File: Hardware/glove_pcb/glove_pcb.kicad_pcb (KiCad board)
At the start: 4 copper layers, 144.6 x 80.7 mm, 124 parts, among them J1 OSTVN02A150, J2 OSTVN02A150, J3 54-00130, J4 0430451000, J5 302-R141, J6 302-R141, J7 61300611121, J8 67997-206HLF, J9 22053061, M1 MountingHole_3.5mm_Pad, M2 MountingHole_3.5mm_Pad, M3 MountingHole_3.5mm_Pad, M4 MountingHole_3.5mm_Pad, U1 AP63205WU, U10 BZA408B, U11 BZA408B, U12 MCP3008, U13 ATmega328PB-A, U14 MCP3008, U15 MCP3008, U16 BM70BLES1FC2-0B04AA, U17 MCP111T-195I/TT, U18 74LVC1T45GW_125, U19 74LVC1T45GW_125, U2 TCR2EF33_LMCT, U3 DRV8876PWPR, U4 DRV8876PWPR, U5 DRV8876PWPR, U6 DRV8876PWPR, U7 DRV8876PWPR, U8 BZA408B, U9 BZA408B

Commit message: More routing re-work and cleanup
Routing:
- net MISO: track 10.1 -> 55.7 mm, vias 0 -> 2
- net +5V: track 124.8 -> 92.8 mm, vias 32 -> 33
- net MOSI: track 17.6 -> 49.3 mm
- net GND: track 269.0 -> 258.5 mm, vias 96 -> 95
- net SCK1: track 152.5 -> 143.8 mm
- net UC_PERIPHERAL_SLEEP_RESET: track 222.6 -> 227.3 mm
- net UC_MOTOR_PH3: track 138.6 -> 135.9 mm, vias 4 -> 6
- net SCK: track 47.0 -> 49.2 mm, vias 4 -> 3
- net POT_AREF: track 53.5 -> 51.6 mm
- net SS_ADC2: track 43.8 -> 45.5 mm, vias 7 -> 6
- net MISO1: track 145.9 -> 147.5 mm
- net SS_ADC1: track 24.8 -> 26.4 mm
- net SS_ADC3: track 69.0 -> 70.1 mm
- net OC1B: track 84.9 -> 83.8 mm
- net OC1A: track 90.0 -> 89.0 mm
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
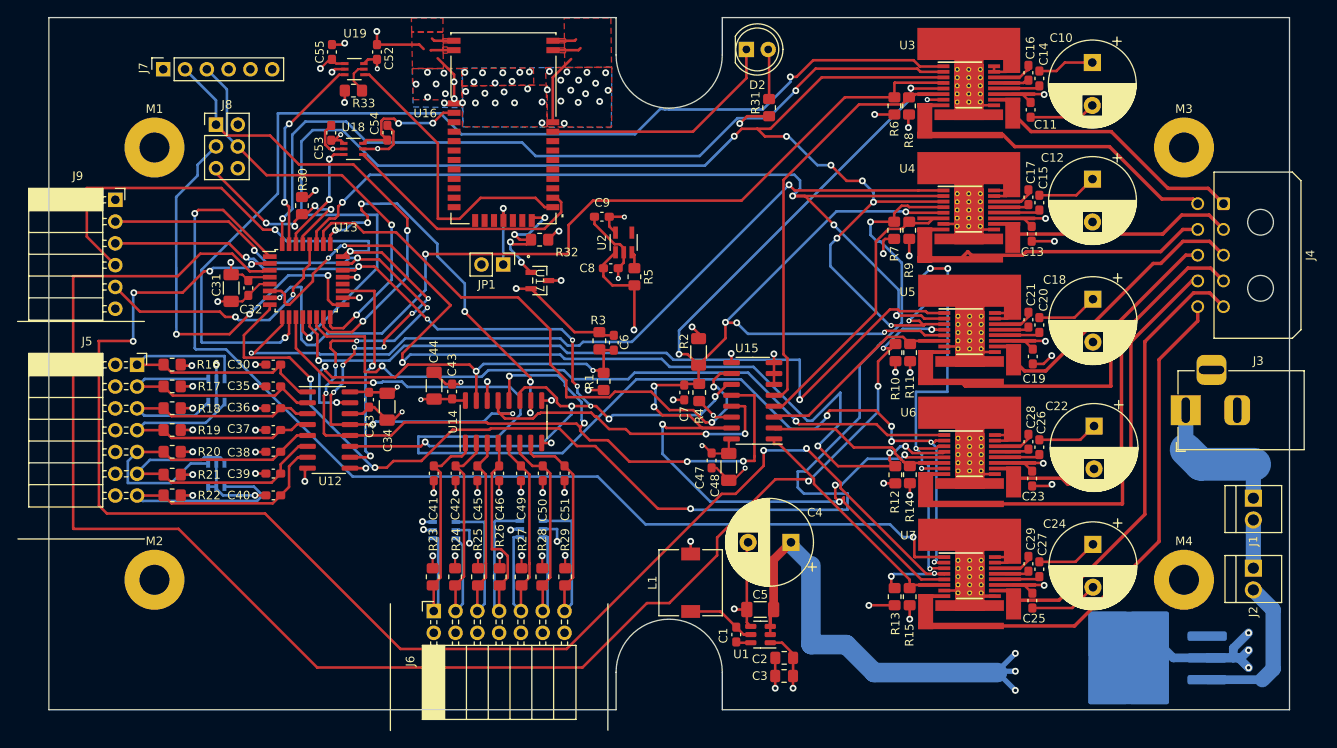
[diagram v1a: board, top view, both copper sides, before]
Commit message: Improving routing to voltage regulators
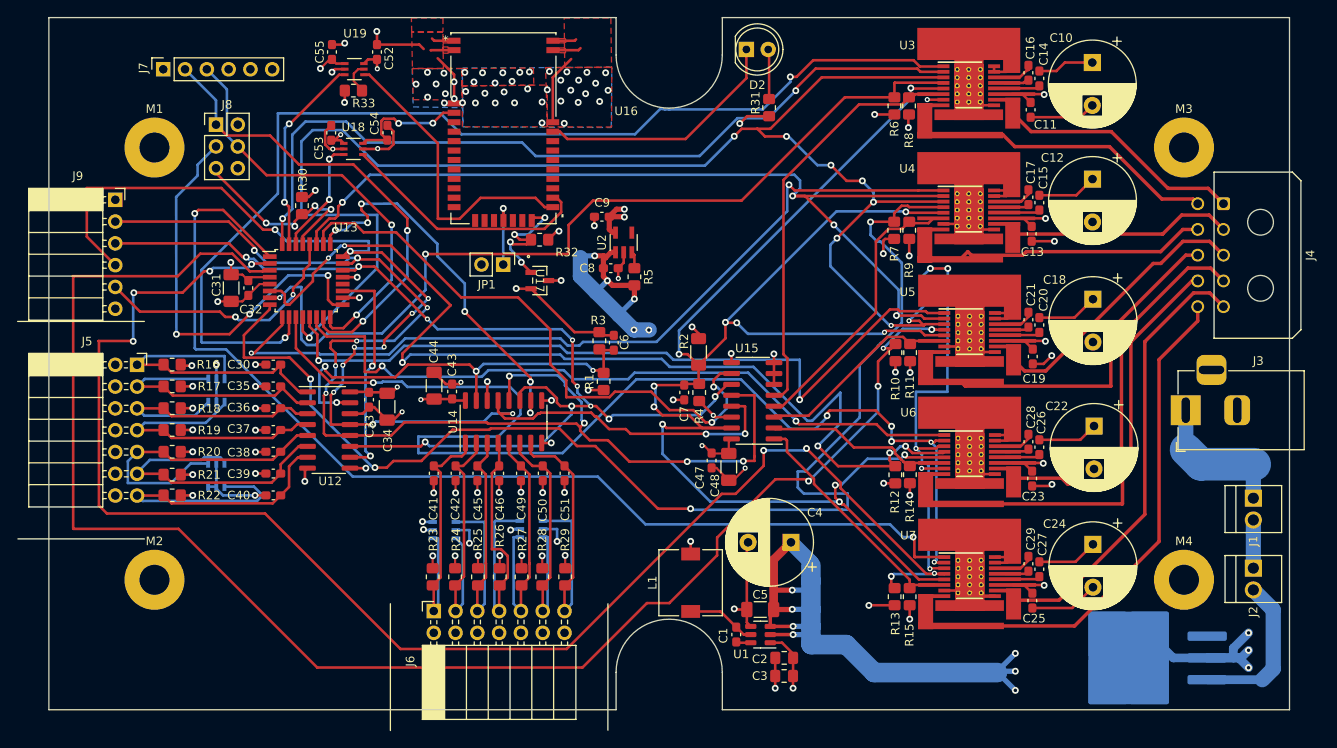
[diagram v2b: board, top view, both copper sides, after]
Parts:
- U16: footprint Glove_Footprints:BM70BLES1FC2_MCH(2) -> Glove_Footprints:BM70BLES1FC2_MCH
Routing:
- net +12V: track 146.7 -> 164.3 mm, vias 11 -> 15
- net +5V: track 92.8 -> 109.9 mm, vias 33 -> 37
- net GND: track 258.5 -> 254.4 mm, vias 95 -> 96
- net +3.3V: track 28.7 -> 31.1 mm, vias 7 -> 8
- net OC0B: track 95.8 -> 97.5 mm
- net MOTOR_AREF: track 201.1 -> 200.4 mm
- net Net-(D2-K): track 28.5 -> 29.2 mm

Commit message: Clearance should be fixed as well as tracks for motors were increased
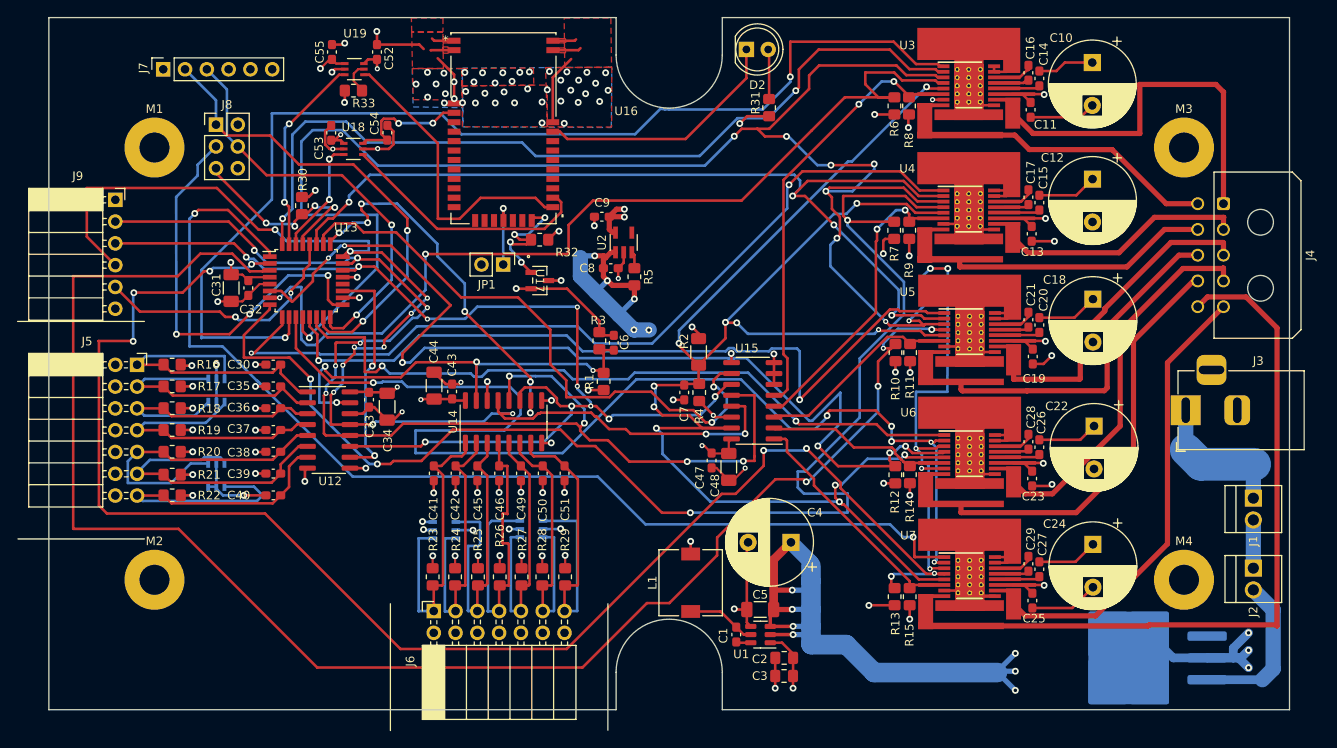
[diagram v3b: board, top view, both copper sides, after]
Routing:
- net MOTOR5_OUT1: track 56.4 -> 82.9 mm
- net MOTOR1_OUT2: track 28.9 -> 44.7 mm
- net UC_PERIPHERAL_SLEEP_RESET: track 227.3 -> 240.9 mm
- net MOTOR2_FAULT: track 147.2 -> 159.4 mm
- net MOTOR1_FAULT: track 103.5 -> 111.1 mm
- net MOTOR3_OUT2: track 31.9 -> 38.4 mm
- net OC0A: track 125.9 -> 129.8 mm
- net MOSI1: track 128.7 -> 132.2 mm
- net POT_MIDDLE_3: track 32.5 -> 35.9 mm
- net POT_PINKY_3: track 37.7 -> 40.7 mm
- net UC_MOTOR_PH1: track 96.0 -> 98.9 mm
- net POT_RING_3: track 35.4 -> 38.3 mm
- net POT_RING_1: track 31.1 -> 33.9 mm
- net POT_PINKY_2: track 31.5 -> 34.2 mm
- net MOTOR2_ISEN: track 32.6 -> 35.0 mm, vias 0 -> 2
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
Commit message: Silkscreen cleanup and final fixes
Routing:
- net MOTOR5_OUT1: track 82.9 -> 57.7 mm
- net POT_MIDDLE_2: track 43.7 -> 36.5 mm
- net MOTOR5_OUT2: track 52.3 -> 56.9 mm
- net GND: track 252.5 -> 250.9 mm, vias 96 -> 93
- net POT_AREF: track 53.3 -> 52.0 mm
- net POT_RING_3: track 38.3 -> 37.3 mm
- net POT_MIDDLE_1: track 34.2 -> 35.1 mm
- net MOTOR3_OUT2: track 38.4 -> 37.6 mm
- net MOTOR4_OUT1: track 47.6 -> 48.2 mm

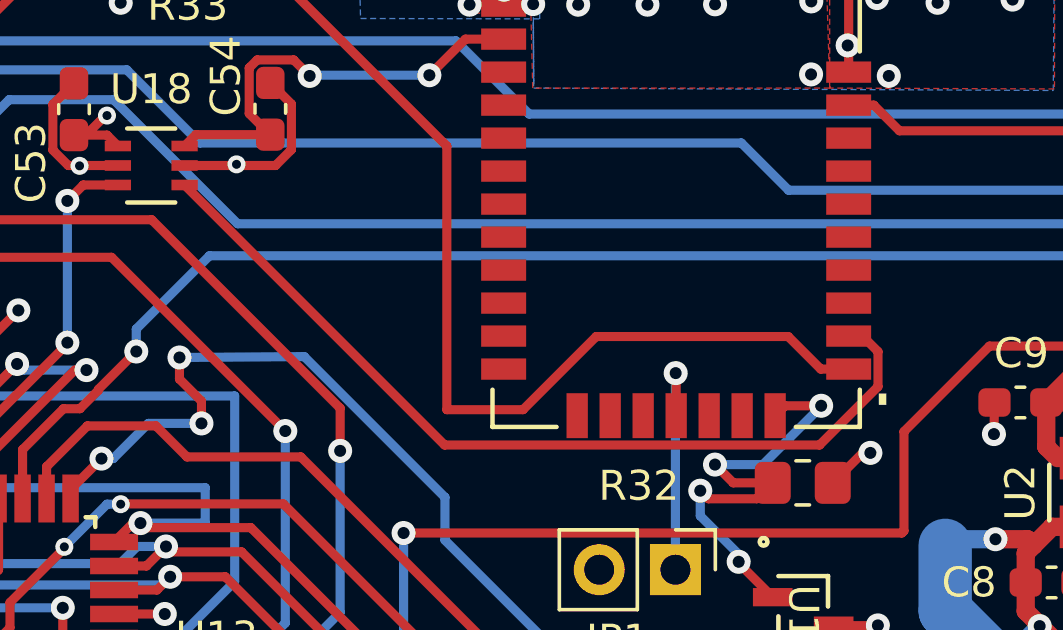
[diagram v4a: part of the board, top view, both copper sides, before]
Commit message: 3V3 RXD track clearance
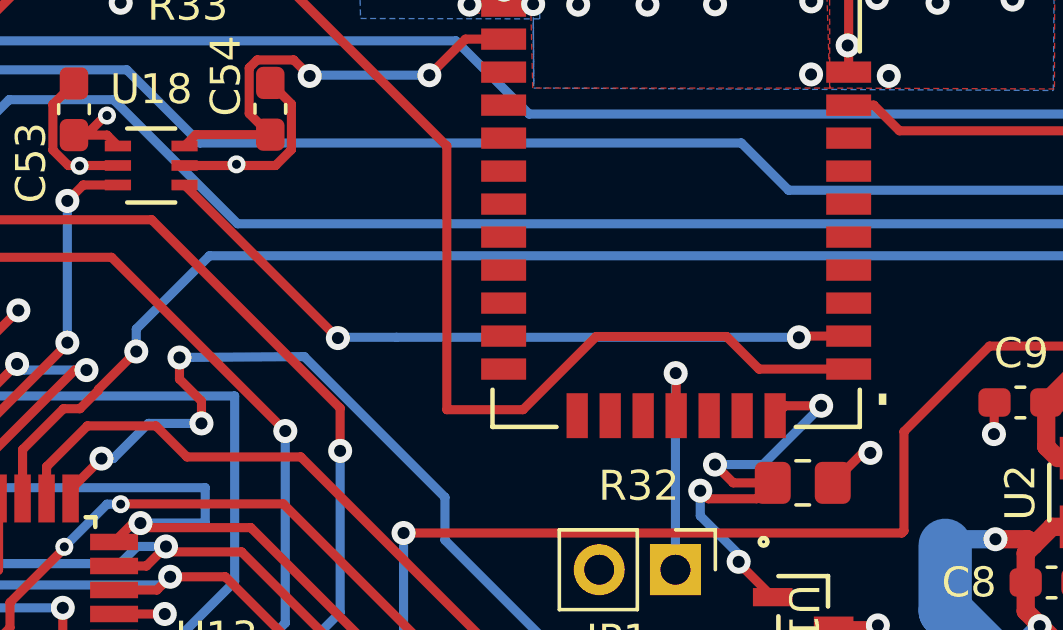
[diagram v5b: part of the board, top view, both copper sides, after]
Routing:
- net 3V3_RXD: track 29.9 -> 25.0 mm, vias 0 -> 2
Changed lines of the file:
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@@
   (segment (start 171.9 118.498202) (end 171.648202 118.75) (width 0.3048) (layer "B.Cu") (net 89))
   (segment (start 113.792 69.9516) (end 113.792 78.74) (width 0.3048) (layer "F.Cu") (net 99))
+  (segment (start 118.7704 76.3016) (end 123.1138 76.3016) (width 0.3048) (layer "F.Cu") (net 99))
+  (segment (start 105.1725 61.949999) (end 105.790399 61.949999) (width 0.3048) (layer "F.Cu") (net 99))
   (segment (start 116.332 78.74) (end 118.7704 76.3016) (width 0.3048) (layer "F.Cu") (net 99))
+  (segment (start 105.790399 61.949999) (end 113.792 69.9516) (width 0.3048) (layer "F.Cu") (net 99))
+  (segment (start 113.792 78.74) (end 116.332 78.74) (width 0.3048) (layer "F.Cu") (net 99))
   (segment (start 127.16882 77.3684) (end 127.18676 77.38634) (width 0.3048) (layer "F.Cu") (net 99))
-  (segment (start 105.1725 61.949999) (end 105.790399 61.949999) (width 0.3048) (layer "F.Cu") (net 99))
-  (segment (start 113.792 78.74) (end 116.332 78.74) (width 0.3048) (layer "F.Cu") (net 99))
-  (segment (start 126.25594 77.38634) (end 127.18676 77.38634) (width 0.3048) (layer "F.Cu") (net 99))
-  (segment (start 118.7704 76.3016) (end 125.1712 76.3016) (width 0.3048) (layer "F.Cu") (net 99))
-  (segment (start 125.1712 76.3016) (end 126.25594 77.38634) (width 0.3048) (layer "F.Cu") (net 99))
-  (segment (start 105.790399 61.949999) (end 113.792 69.9516) (width 0.3048) (layer "F.Cu") (net 99))
-  (segment (start 128.16446 77.97034) (end 128.16446 76.80234) (width 0.3048) (layer "F.Cu") (net 100))
-  (segment (start 126.21755 79.91725) (end 128.16446 77.97034) (width 0.3048) (layer "F.Cu") (net 100))
-  (segment (start 105.05 71.25) (end 113.71725 79.91725) (width 0.3048) (layer "F.Cu") (net 100))
-  (segment (start 128.16446 76.80234) (end 127.64864 76.28652) (width 0.3048) (layer "F.Cu") (net 100))
-  (segment (start 113.71725 79.91725) (end 126.21755 79.91725) (width 0.3048) (layer "F.Cu") (net 100))
+  (segment (start 124.19854 77.38634) (end 127.18676 77.38634) (width 0.3048) (layer "F.Cu") (net 99))
+  (segment (start 123.1138 76.3016) (end 124.19854 77.38634) (width 0.3048) (layer "F.Cu") (net 99))
+  (segment (start 105.05 71.25) (end 110.1524 76.3524) (width 0.3048) (layer "F.Cu") (net 100))
+  (segment (start 125.77048 76.28652) (end 125.5268 76.327) (width 0.3048) (layer "F.Cu") (net 100))
+  (segment (start 110.1598 76.3524) (end 110.1598 76.3598) (width 0.3048) (layer "F.Cu") (net 100))
+  (segment (start 110.1524 76.3524) (end 110.1598 76.3524) (width 0.3048) (layer "F.Cu") (net 100))
+  (segment (start 127.18676 76.28652) (end 125.77048 76.28652) (width 0.3048) (layer "F.Cu") (net 100))
   (segment (start 127.64864 76.28652) (end 127.18676 76.28652) (width 0.3048) (layer "F.Cu") (net 100))
+  (segment (start 125.5268 76.327) (end 125.7554 76.3016) (width 0.3048) (layer "F.Cu") (net 100))
+  (via (at 110.1598 76.3524) (size 0.8) (drill 0.4) (layers "F.Cu" "B.Cu") (net 100))
+  (via (at 125.5268 76.327) (size 0.8) (drill 0.4) (layers "F.Cu" "B.Cu") (net 100))
+  (segment (start 112.1156 76.327) (end 110.1598 76.327) (width 0.3048) (layer "B.Cu") (net 100))
+  (segment (start 125.5268 76.327) (end 112.1156 76.327) (width 0.3048) (layer "B.Cu") (net 100))
+  (segment (start 110.1598 76.327) (end 110.1344 76.3524) (width 0.3048) (layer "B.Cu") (net 100))
   (zone (net 3) (net_name "GND") (layer "F.Cu") (hatch edge 0.5)
     (priority 4)

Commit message: Minor changes in the morning before meeting
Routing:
- net MOTOR3_OUT1: track 39.3 -> 36.3 mm
- net RST: track 24.6 -> 26.9 mm
- net GND: track 250.9 -> 249.1 mm
- net SCK1: track 143.6 -> 142.0 mm
- net MOTOR4_OUT1: track 48.2 -> 46.7 mm
- net MOTOR2_OUT1: track 30.5 -> 29.1 mm
- net UC_MOTOR_PH1: track 98.9 -> 100.1 mm
- net MOTOR3_OUT2: track 37.6 -> 36.5 mm
- net +3.3V: track 31.1 -> 31.8 mm
- net +5V: track 109.9 -> 110.6 mm
- net MISO1: track 146.1 -> 145.4 mm
